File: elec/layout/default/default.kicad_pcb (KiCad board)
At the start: 2 copper layers, 45 x 167 mm, 132 parts, among them U10 1kΩ ±1% 62.5mW, U11 1kΩ ±1% 62.5mW, U12 1kΩ ±1% 62.5mW, U13 1kΩ ±1% 62.5mW, U14 1kΩ ±1% 62.5mW, U15 1kΩ ±1% 62.5mW, U16 1kΩ ±1% 62.5mW, U17 1kΩ ±1% 62.5mW, U18 1kΩ ±1% 62.5mW, U7 1kΩ ±1% 62.5mW, U8 1kΩ ±1% 62.5mW, U9 1kΩ ±1% 62.5mW

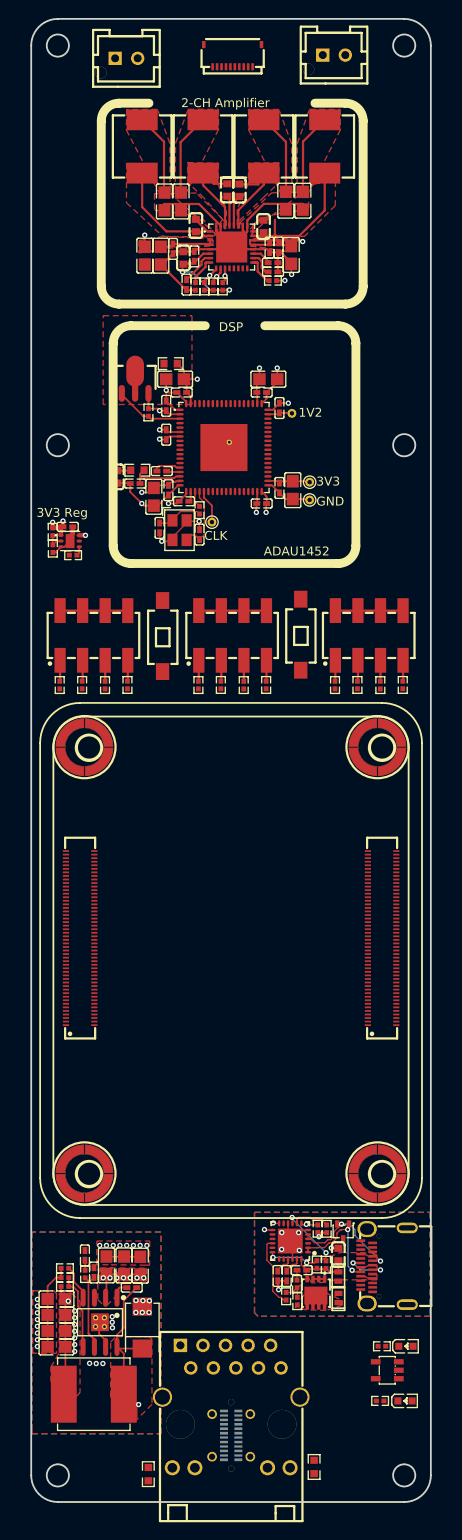
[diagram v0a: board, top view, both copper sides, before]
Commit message: cleanup old parts
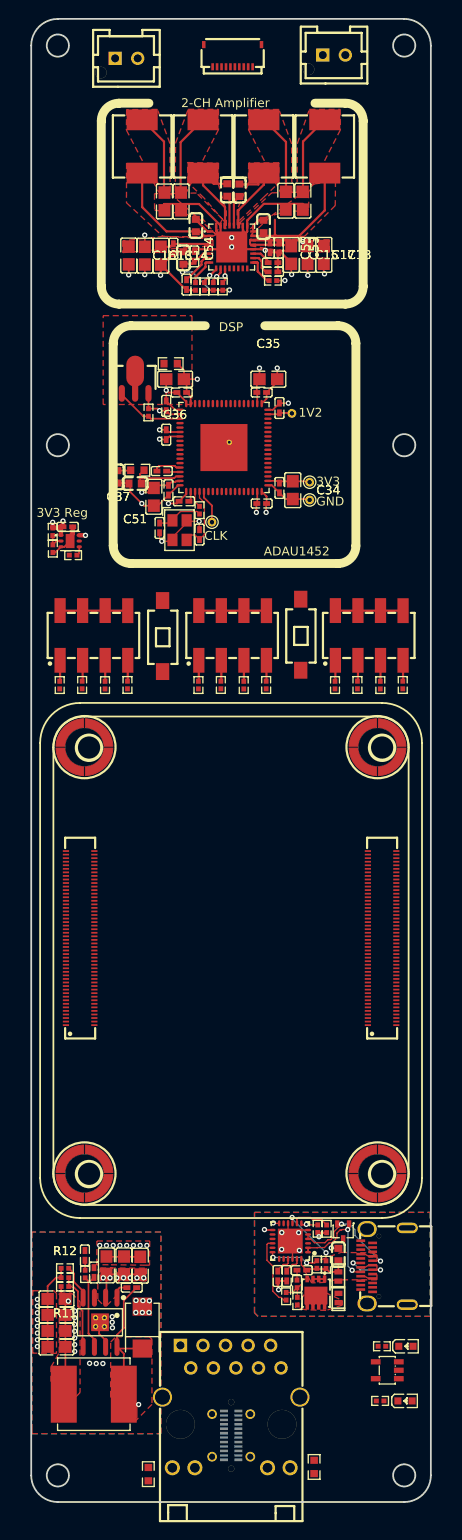
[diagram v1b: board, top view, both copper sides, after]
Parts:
- added C53: 100nF ±10% 16V X7R, Samsung_Electro_Mechanics_CL05B104KO5NNNC:C0402, F.Cu at (154.6, 48.9)
- added C54: 100nF ±10% 16V X7R, Samsung_Electro_Mechanics_CL05B104KO5NNNC:C0402, F.Cu at (142.7, 48.9)
- added C55: 100nF ±10% 16V X7R, Samsung_Electro_Mechanics_CL05B104KO5NNNC:C0402, F.Cu at (153.6, 48.8)
- C13, C14, C15: value 22µF ±20% 25V X5R -> 10µF ±10% 16V X5R; footprint Samsung_Electro_Mechanics_CL21A226MAQNNNE:C0805 -> Samsung_Electro_Mechanics_CL21A106KOQNNNE:C0805
- C16, C17, C18: value 100nF ±10% 16V X7R -> 10µF ±10% 16V X5R; footprint Samsung_Electro_Mechanics_CL05B104KO5NNNC:C0402 -> Samsung_Electro_Mechanics_CL21A106KOQNNNE:C0805
- C34, C35, C36, C37: value 10µF ±10% 25V X5R -> 10µF ±10% 16V X5R; footprint Samsung_Electro_Mechanics_CL21A106KAYNNNE:C0805 -> Samsung_Electro_Mechanics_CL21A106KOQNNNE:C0805
- C51: footprint FH_0402B151K500NT:C0402 -> FH_0603B151K500NT:C0603
- R11: value 10kΩ ±1% 62.5mW -> 20kΩ ±1% 62.5mW; footprint UNI_ROYAL_0402WGF1002TCE:R0402 -> UNI_ROYAL_0402WGF2002TCE:R0402
- R12: value 10kΩ ±1% 62.5mW -> 100kΩ ±1% 62.5mW; footprint UNI_ROYAL_0402WGF1002TCE:R0402 -> UNI_ROYAL_0402WGF1003TCE:R0402
- moved C18 6.16 mm to (159.6, 49.6)
- moved C16 5.04 mm to (137.7, 49.7)
- moved C17 3.37 mm to (157.8, 49.6)
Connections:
- CN1 pad 13: line-7 -> line-12
- CN1 pad 23: cm5-pins[45] -> pins[45]
- CN1 pad 25: line-9 -> line-7
- CN1 pad 73: line-11 -> line-9
- CN1 pad 75: line-12 -> line-10
- CN1 pad 76: line-10 -> line-11
- CN1 pad 77: cm5-pins[46] -> pins[46]
- FPC1 pad 1: pins[57] -> pins[46]
- FPC1 pad 10: line-7 -> pins[57]
- FPC1 pad 2: line -> pins[45]
- FPC1 pad 3: hv-2 -> line-7
- FPC1 pad 4: gnd -> line-8
- FPC1 pad 5: hv -> gnd
- FPC1 pad 6: gnd -> hv
- FPC1 pad 7: line-8 -> gnd
- FPC1 pad 8: line-9 -> hv-2
- FPC1 pad 9: line-10 -> line
- U24 pad 57: line-10 -> line-11
- U24 pad 58: line-7 -> line-12
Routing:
- net gnd: track 160.5 -> 167.7 mm, vias 46 -> 54
- added copper zone on F.Cu, net line-5
- added copper zone on F.Cu, net line-6

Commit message: remove fabll nonos
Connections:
- CN1 pad 13: line-12 -> line-10
- CN1 pad 25: line-7 -> pins[49]
- CN1 pad 73: line-9 -> line-7
- CN1 pad 75: line-10 -> line-8
- CN1 pad 76: line-11 -> line-9
- CN1 pad 86: line-8 -> pins[28]
- CN1 pad 88: line-13 -> line-11
- CN2 pad 25: pins[49] -> cm5.cm5.hdi_b-pins[49]
- CN2 pad 86: pins[28] -> cm5.cm5.hdi_b-pins[28]
- FPC1 pad 3: line-7 -> pins[49]
- FPC1 pad 4: line-8 -> pins[28]
- U24 pad 57: line-11 -> line-9
- U24 pad 58: line-12 -> line-10
- U24 pad 59: line-13 -> line-11
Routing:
- net cm5-pins[16]: track 30.1 -> 0.00 mm
- net cm5-pins[14]: track 26.8 -> 0.00 mm
- net cm5-pins[9]: track 20.5 -> 0.00 mm
- net cm5-pins[5]: track 19.7 -> 0.00 mm
- net cm5-pins[2]: track 19.4 -> 0.00 mm
- net cm5-pins[4]: track 18.5 -> 0.00 mm
- net cm5-pins[3]: track 18.0 -> 0.00 mm
- net cm5-pins[11]: track 17.2 -> 0.00 mm
- net cm5-pins[8]: track 15.5 -> 0.00 mm
- net cm5-pins[10]: track 14.0 -> 0.00 mm
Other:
- copper layers 2 -> 4

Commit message: layout mostly complete
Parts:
- removed U10, U11, U12, U13, U14, U15, U16, U17, U18, U7, U8, U9: 1kΩ ±1% 62.5mW, UNI_ROYAL_0402WGF1001TCE:R0402
- added C56: , Honor_Elec_RVT1H470M0607:CAP-SMD_BD6.3-L6.6-W6.6-FD, F.Cu at (130.6, 48.0)
- added C57: , Honor_Elec_RVT1H470M0607:CAP-SMD_BD6.3-L6.6-W6.6-FD, F.Cu at (130.6, 38.8)
- added C58: , Honor_Elec_RVT1H470M0607:CAP-SMD_BD6.3-L6.6-W6.6-FD, F.Cu at (168.2, 49.0)
- added C59: , Honor_Elec_RVT1H470M0607:CAP-SMD_BD6.3-L6.6-W6.6-FD, F.Cu at (168.1, 39.6)
- added R28: 1kΩ ±1% 62.5mW, UNI_ROYAL_0402WGF1001TCE:R0402, F.Cu at (160.8, 97.9)
- added R29: 1kΩ ±1% 62.5mW, UNI_ROYAL_0402WGF1001TCE:R0402, F.Cu at (163.4, 97.9)
- added R30: 1kΩ ±1% 62.5mW, UNI_ROYAL_0402WGF1001TCE:R0402, F.Cu at (165.9, 97.9)
- added R31: 1kΩ ±1% 62.5mW, UNI_ROYAL_0402WGF1001TCE:R0402, F.Cu at (168.4, 97.9)
- added R32: 1kΩ ±1% 62.5mW, UNI_ROYAL_0402WGF1001TCE:R0402, F.Cu at (145.4, 97.9)
- added R33: 1kΩ ±1% 62.5mW, UNI_ROYAL_0402WGF1001TCE:R0402, F.Cu at (147.9, 97.9)
- added R34: 1kΩ ±1% 62.5mW, UNI_ROYAL_0402WGF1001TCE:R0402, F.Cu at (150.4, 97.9)
- added R35: 1kΩ ±1% 62.5mW, UNI_ROYAL_0402WGF1001TCE:R0402, F.Cu at (152.9, 97.9)
- added R36: 1kΩ ±1% 62.5mW, UNI_ROYAL_0402WGF1001TCE:R0402, F.Cu at (130.2, 97.7)
- added R37: 1kΩ ±1% 62.5mW, UNI_ROYAL_0402WGF1001TCE:R0402, F.Cu at (132.7, 97.7)
- added R38: 1kΩ ±1% 62.5mW, UNI_ROYAL_0402WGF1001TCE:R0402, F.Cu at (135.2, 97.7)
- added R39: 1kΩ ±1% 62.5mW, UNI_ROYAL_0402WGF1001TCE:R0402, F.Cu at (137.8, 97.7)
- moved D2 4.66 mm to (167.8, 177.1)
- moved R7 4.62 mm to (165.2, 177.0)
- moved U2 4.34 mm to (166.5, 179.6)
- moved D1 3.43 mm to (167.8, 175.4)
- moved R6 3.38 mm to (165.2, 175.4)
- moved U21 0.63 mm to (137.4, 26.9)
- moved HDR3 0.28 mm to (134.0, 92.4)
- moved U22 0.27 mm to (160.7, 26.9)
- moved HDR2 0.20 mm to (149.2, 92.5)
- moved HDR1 0.13 mm to (164.6, 92.6)
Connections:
- net A5 renamed cc0
- net B5 renamed cc1
- net cm5-pins[10] renamed eth2_P
- net cm5-pins[11] renamed eth0_P
- net cm5-pins[2] renamed eth3_P
- net cm5-pins[2]-1 renamed pins[2]
- net cm5-pins[3] renamed eth1_P
- net cm5-pins[4] renamed eth3_N
- net cm5-pins[4]-1 renamed pins[4]
- net cm5-pins[5] renamed eth1_N
- net cm5-pins[8] renamed eth2_N
- net cm5-pins[9] renamed eth0_N
- net cm5.cm5-pins[44]-1 renamed pins[44]
- net cm5.cm5.hdi_b-pins[10] renamed pins[10]
- net cm5.cm5.hdi_b-pins[11] renamed pins[11]
- net cm5.cm5.hdi_b-pins[3] renamed pins[3]
- net cm5.cm5.hdi_b-pins[40] renamed pins[40]
- net cm5.cm5.hdi_b-pins[5] renamed pins[5]
- net cm5.cm5.hdi_b-pins[8] renamed pins[8]
- net cm5.cm5.hdi_b-pins[9] renamed pins[9]
- net hv renamed 3v3_vcc
- net hv-1 renamed 20v_vcc
- net hv-2 renamed 5v_vcc
- net line-5 renamed spkr_tweet_n
- net line-6 renamed spkr_tweet_p
- net nPDN renamed amp_pdn
- net nRESET renamed dsp_reset_disable
- C7 pad 1: line-3 -> spkr_full_n
- C8 pad 1: line-4 -> spkr_full_p
- CN1 pad 13: line-10 -> line-3
- CN1 pad 17: pins[33] -> amp_fault
- CN1 pad 18: line-2 -> i2c0_sda
- CN1 pad 23: pins[45] -> touch_interrupt
- CN1 pad 25: pins[49] -> nfc_interrupt
- CN1 pad 27: pins[53] -> cm5.cm5-pins[53]
- CN1 pad 28: line -> i2c1_scl
- CN1 pad 29: pins[57] -> i2c1_sda
- CN1 pad 73: line-7 -> line
- CN1 pad 75: line-8 -> line-1
- CN1 pad 76: line-9 -> line-2
- CN1 pad 77: pins[46] -> led_data
- CN1 pad 78: cm5.cm5-pins[44] -> amp_mute
- CN1 pad 80: cm5.cm5-pins[40] -> amp_warn
- CN1 pad 83: line-1 -> i2c0_scl
- CN1 pad 86: pins[28] -> nfc_reset
- CN1 pad 88: line-11 -> line-4
- CN2 pad 17: cm5-pins[33] -> pins[33]
- CN2 pad 23: cm5.cm5-pins[45] -> pins[45]
- CN2 pad 25: cm5.cm5.hdi_b-pins[49] -> pins[49]
- CN2 pad 27: cm5.cm5-pins[53] -> cm5.cm5-pins[53]-1
- CN2 pad 29: cm5.cm5-pins[57] -> pins[57]
- CN2 pad 77: cm5.cm5-pins[46] -> pins[46]
- CN2 pad 86: cm5.cm5.hdi_b-pins[28] -> pins[28]
- FPC1 pad 1: pins[46] -> led_data
- FPC1 pad 10: pins[57] -> i2c1_sda
- FPC1 pad 2: pins[45] -> touch_interrupt
- FPC1 pad 3: pins[49] -> nfc_interrupt
- FPC1 pad 4: pins[28] -> nfc_reset
- FPC1 pad 9: line -> i2c1_scl
- L1 pad 2: line-3 -> spkr_full_n
- L2 pad 2: line-4 -> spkr_full_p
- R15 pad 1: line-1 -> i2c0_scl
- R16 pad 1: line-2 -> i2c0_sda
- R2 pad 1: pins[33] -> amp_fault
- R3 pad 1: line -> amp_mute
- R5 pad 1: pins[53] -> amp_warn
- U1 pad 10: line -> amp_mute
- U1 pad 11: pins[53] -> amp_warn
- U1 pad 15: line-2 -> i2c0_sda
- U1 pad 16: line-1 -> i2c0_scl
- U1 pad 9: pins[33] -> amp_fault
- U19 pad : regulator_5v.ic.footprint.pins[0].net-net -> gnd
- U20 pad 7: line-1 -> i2c0_scl
- U20 pad 8: line-2 -> i2c0_sda
- U21 pad 1: line-4 -> spkr_full_p
- U21 pad 2: line-3 -> spkr_full_n
- U23 pad A6: A6 -> usb_connector-A6
- U23 pad A7: A7 -> usb_connector-A7
- U23 pad B6: A6 -> usb_connector-A6
- U23 pad B7: A7 -> usb_connector-A7
- U24 pad 28: line-1 -> i2c0_scl
- U24 pad 29: line-2 -> i2c0_sda
- U24 pad 30: line-2 -> i2c0_sda
- U24 pad 31: line-1 -> i2c0_scl
- U24 pad 57: line-9 -> line-2
- U24 pad 58: line-10 -> line-3
- U24 pad 59: line-11 -> line-4
- USB1 pad A6: A6 -> pd_controller-A6
- USB1 pad A7: A7 -> pd_controller-A7
- USB1 pad B6: A6 -> pd_controller-A6
- USB1 pad B7: A7 -> pd_controller-A7
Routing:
- net 5v_vcc: track 13.1 -> 245.4 mm, vias 9 -> 19
- net 20v_vcc: track 25.0 -> 239.1 mm, vias 9 -> 29
- net i2c0_scl: track 0.00 -> 170.0 mm, vias 0 -> 7
- net i2c0_sda: track 0.00 -> 156.7 mm, vias 0 -> 4
- net nfc_reset: track 0.00 -> 132.6 mm, vias 0 -> 3
- net led_data: track 0.00 -> 130.6 mm, vias 0 -> 3
- net touch_interrupt: track 0.00 -> 124.8 mm, vias 0 -> 2
- net nfc_interrupt: track 0.00 -> 122.0 mm, vias 0 -> 2
- net i2c1_sda: track 0.00 -> 119.4 mm, vias 0 -> 2
- net i2c1_scl: track 0.00 -> 119.0 mm, vias 0 -> 2
- net amp_warn: track 0.00 -> 116.0 mm, vias 0 -> 4
- net amp_fault: track 0.00 -> 113.6 mm, vias 0 -> 3
- net amp_mute: track 0.00 -> 113.5 mm, vias 0 -> 4
- net amp_pdn: track 3.34 -> 107.6 mm, vias 0 -> 2
- net line-2: track 4.26 -> 107.8 mm, vias 0 -> 5
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- added copper zone on B.Cu, net 3v3_vcc
- added copper zone on In1.Cu, net 3v3_vcc
- added copper zone on In1.Cu, net VBUS
- added copper zone on In2.Cu, net VBUS
- added copper zone on In2.Cu, net gnd
- added copper zone on F.Cu, net spkr_full_n
- added copper zone on F.Cu, net spkr_full_p
- removed copper zone on F.Cu, net line-3
- removed copper zone on F.Cu, net line-4
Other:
- board text added: "CH0"
- board text added: "CH1"
- board text added: "CH2"
- board text added: "CH3"
- board text added: "Full Range"
- board text added: "Tweeter"

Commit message: layout complete
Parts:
- added R40: 10kΩ ±1% 62.5mW, UNI_ROYAL_0402WGF1002TCE:R0402, F.Cu at (154.2, 79.9)
- added R41: 10kΩ ±1% 62.5mW, UNI_ROYAL_0402WGF1002TCE:R0402, F.Cu at (154.2, 80.9)
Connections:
- net LRCLK renamed amp_i2s_ws
- net SCLK renamed amp_i2s_sck
- net SDIN renamed amp_i2s_sd
- net cm5-pins[92] renamed boot_mode
- net cm5.cm5.hdi_b-pins[92] renamed pins[92]
- net line renamed uart0_tx
- net line-1 renamed uart0_rx
- net line-2 renamed i2s_sck
- net line-3 renamed i2s_ws
- net pins[91] renamed power_button
- CN1 pad 88: line-4 -> i2s_sd
- R30 pad 1: debug_headers[0]-line -> 5v_vcc
- R31 pad 1: debug_headers[0]-line-1 -> 3v3_vcc
- R38 pad 1: 5v_vcc -> i2s_sd
- RJ1 pad : cm5.rj45.connector.footprint.pins[0].net-net -> (no net)
- U21 pad : full_range_speaker_connector.footprint.pins[0].net-net -> (no net)
- U22 pad : tweeter_speaker_connector.footprint.pins[0].net-net -> (no net)
- U23 pad : usb_connector.connector.footprint.pins[0].net-net -> (no net)
- U24 pad 28: i2c0_scl -> SCL_M_SCLK_M_MP2
- U24 pad 29: i2c0_sda -> SDA_M_MISO_M_MP3
- U24 pad 59: line-4 -> i2s_sd
- U3 pad : cm5.stud1.footprint.pins[0].net-net -> (no net)
- U4 pad : cm5.stud2.footprint.pins[0].net-net -> (no net)
- U5 pad : cm5.stud3.footprint.pins[0].net-net -> (no net)
- U6 pad : cm5.stud4.footprint.pins[0].net-net -> (no net)
- USB1 pad : pd_controller.usb_connector.footprint.pins[0].net-net -> (no net)
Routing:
- net i2s_sd: track 0.00 -> 104.9 mm, vias 0 -> 5
- net line-4: track 89.2 -> 0.00 mm, vias 3 -> 0
- net cm5.rj45.connector.footprint.pins[0].net-net: track 22.4 -> 0.00 mm
- net 5v_vcc: track 245.4 -> 253.6 mm, vias 19 -> 18
- net MOSI_ADDR1: track 0.00 -> 6.31 mm
- net SS_ADDR0: track 0.00 -> 5.44 mm
- net gnd: track 258.3 -> 263.3 mm, vias 64 -> 66
- net i2c0_sda: track 156.7 -> 160.6 mm
- net 3v3_vcc: track 60.2 -> 63.4 mm, vias 19 -> 21
- net i2c0_scl: track 170.0 -> 173.2 mm
- added copper zone on F.Cu, net regulator_5v.ic.footprint.pins[0].net-net
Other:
- outline, holes or cut-outs redrawn
- board text added: "5V"
- board text added: "RX"
- board text added: "SCK"
- board text added: "SCL"
- board text added: "SD"
- board text added: "SDA"
- board text added: "TX"
- board text added: "WS"
- board text added: "{{GITHASH}}"
- board text removed: "CH0"
- board text removed: "CH1"
- board text removed: "CH2"
- board text removed: "CH3"

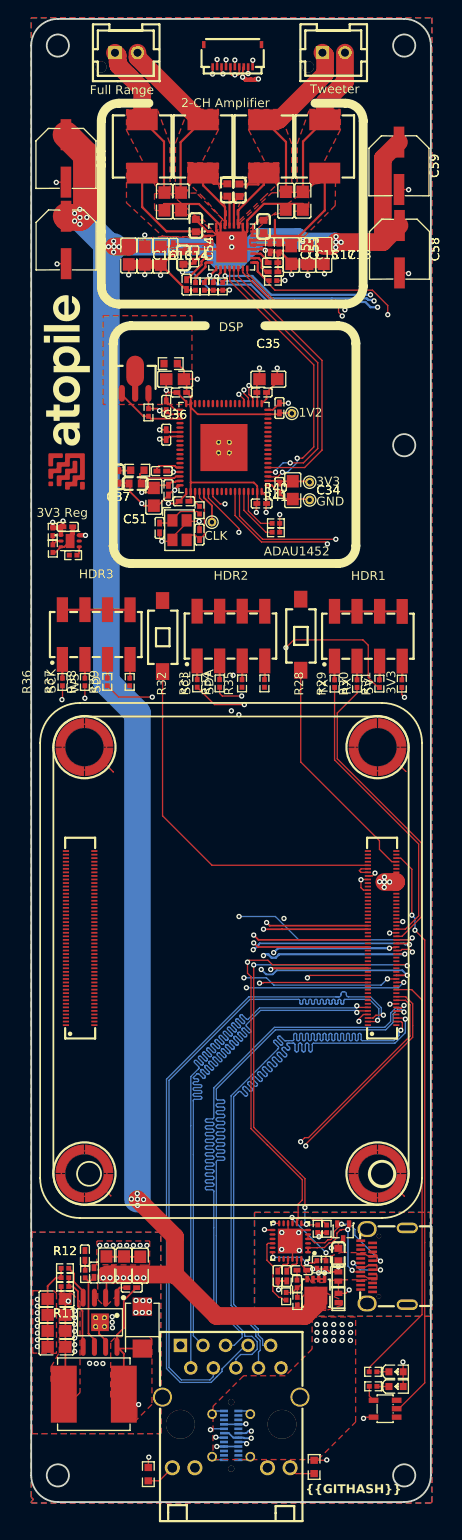
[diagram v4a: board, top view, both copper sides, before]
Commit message: add ethernet sync pin, tidy up layout, remove auto generated from manually modified footprint
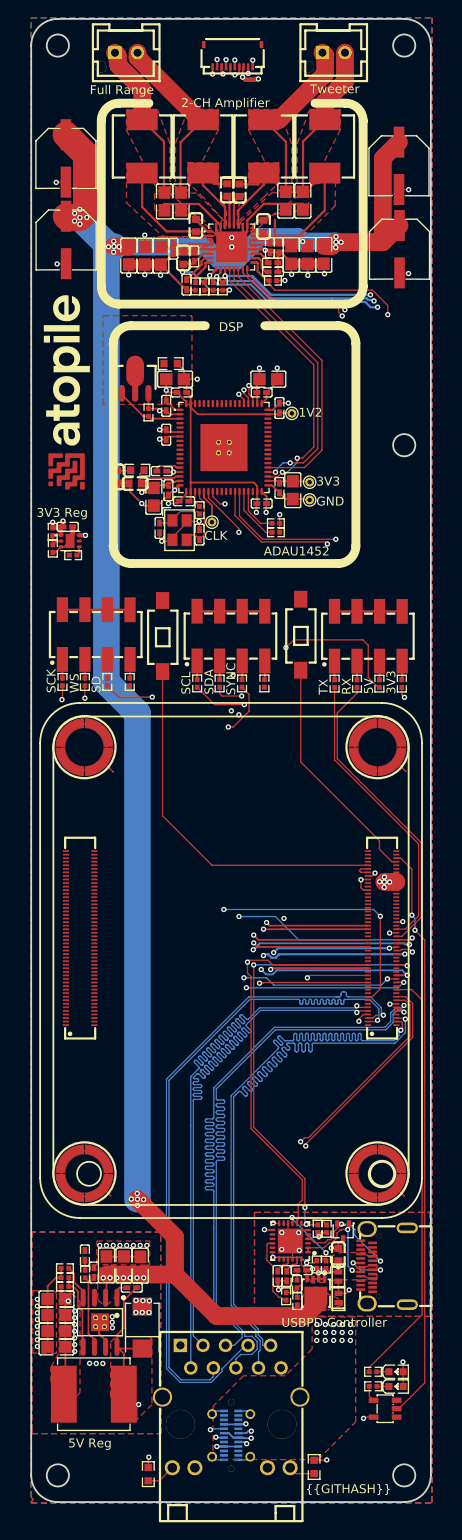
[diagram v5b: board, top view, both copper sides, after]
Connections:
- net cm5.cm5.hdi_b-pins[17] renamed pins[17]
- CN1 pad 9: cm5.cm5.hdi_a-pins[17] -> eth_sync_out
- R34 pad 1: debug_headers[1]-line -> eth_sync_out
- R35 pad 1: debug_headers[1]-line-1 -> debug_headers[1]-line
- RJ1 pad : (no net) -> cm5.rj45.connector.footprint.pins[0].net-net
- U21 pad : (no net) -> full_range_speaker_connector.footprint.pins[0].net-net
- U22 pad : (no net) -> tweeter_speaker_connector.footprint.pins[0].net-net
- U23 pad : (no net) -> usb_connector.connector.footprint.pins[0].net-net
- U3 pad : (no net) -> cm5.stud1.footprint.pins[0].net-net
- U4 pad : (no net) -> cm5.stud2.footprint.pins[0].net-net
- U5 pad : (no net) -> cm5.stud3.footprint.pins[0].net-net
- U6 pad : (no net) -> cm5.stud4.footprint.pins[0].net-net
- USB1 pad : (no net) -> pd_controller.usb_connector.footprint.pins[0].net-net
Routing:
- net eth_sync_out: track 0.00 -> 55.2 mm, vias 0 -> 3
- removed copper zone on F.Cu, net regulator_5v.ic.footprint.pins[0].net-net
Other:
- board text added: "5V Reg"
- board text added: "SYNC"
- board text added: "USBPD Controller"
